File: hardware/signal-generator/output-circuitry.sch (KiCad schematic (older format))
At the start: 57 parts, among them Q1 MMBF5485, Q2 MMBF5485, Q3 MMBF5485, U15 MCP4551-103E/MS, U16 AD8021ARZ, U17 AD8021ARZ, U18 MCP4716, U19 AD8021ARZ, U20 MIC6211, U21 AZ431AN-A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

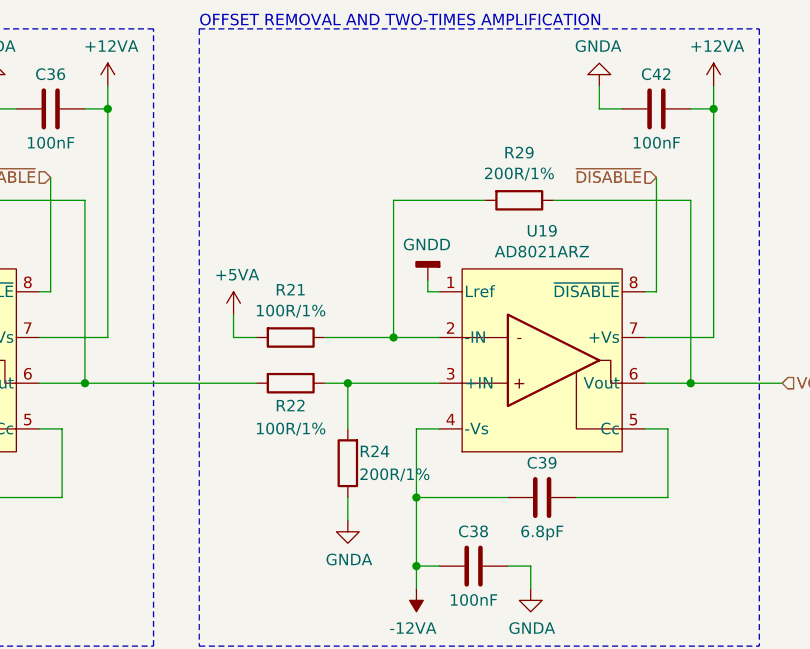
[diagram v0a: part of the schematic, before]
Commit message: [Hardware] Change values of R21, R22, R24, R29
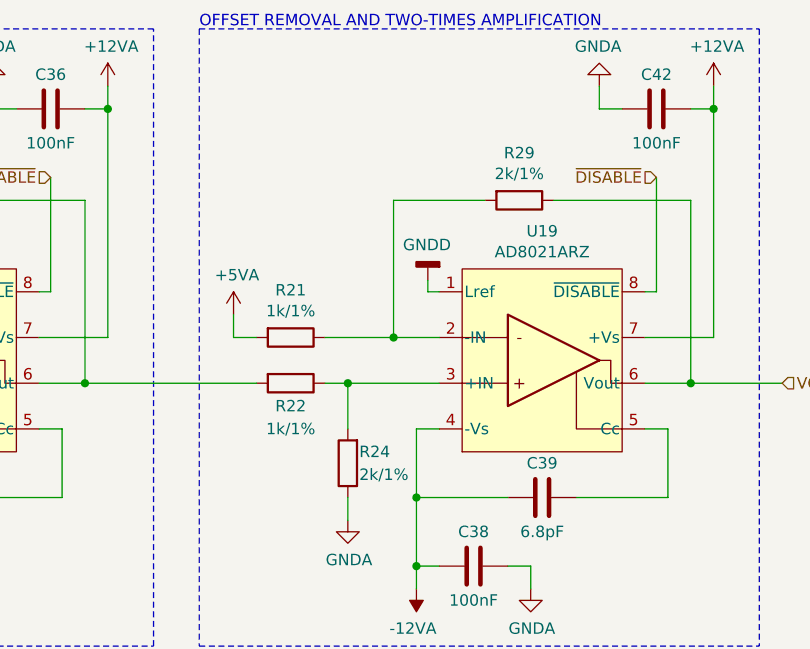
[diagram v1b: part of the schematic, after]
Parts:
- R21, R22: value 100R/1% -> 1k/1%
- R24, R29: value 200R/1% -> 2k/1%
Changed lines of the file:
@@
 Sheet 4 5
 Title "Digital Function Generator v2 - Output Circuitry"
-Date "2019-12-30"
+Date "2020-03-12"
 Rev "1"
 Comp "Petar Nikolov"
@@
 P 6450 4550
 F 0 "R29" V 6243 4550 50  0000 C CNN
-F 1 "200R/1%" V 6334 4550 50  0000 C CNN
+F 1 "2k/1%" V 6334 4550 50  0000 C CNN
 F 2 "Resistors_SMD:R_0805_HandSoldering" V 6380 4550 50  0001 C CNN
 F 3 "~" H 6450 4550 50  0001 C CNN
@@
 P 5450 5150
 F 0 "R21" V 5243 5150 50  0000 C CNN
-F 1 "100R/1%" V 5334 5150 50  0000 C CNN
+F 1 "1k/1%" V 5334 5150 50  0000 C CNN
 F 2 "Resistors_SMD:R_0805_HandSoldering" V 5380 5150 50  0001 C CNN
 F 3 "~" H 5450 5150 50  0001 C CNN
@@
 P 5700 5700
 F 0 "R24" H 5650 5650 50  0000 R CNN
-F 1 "200R/1%" H 5650 5750 50  0000 R CNN
+F 1 "2k/1%" H 5650 5750 50  0000 R CNN
 F 2 "Resistors_SMD:R_0805_HandSoldering" V 5630 5700 50  0001 C CNN
 F 3 "~" H 5700 5700 50  0001 C CNN
@@
 P 5450 5350
 F 0 "R22" V 5550 5350 50  0000 C CNN
-F 1 "100R/1%" V 5650 5350 50  0000 C CNN
+F 1 "1k/1%" V 5650 5350 50  0000 C CNN
 F 2 "Resistors_SMD:R_0805_HandSoldering" V 5380 5350 50  0001 C CNN
 F 3 "~" H 5450 5350 50  0001 C CNN
